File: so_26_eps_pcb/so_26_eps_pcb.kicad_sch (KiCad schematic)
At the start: 0 parts

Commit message: schematic: updated title block
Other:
- company: (none) -> Katharina Nilssen
- title: (none) -> so_26_eps_pcb
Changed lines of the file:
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@@
 	(generator_version "9.0")
 	(paper "A4")
+	(title_block
+		(title "so_26_eps_pcb")
+		(date "2026-01-28")
+		(rev "1")
+		(company "Katharina Nilssen")
+	)
 	(sheet_instances
 		(path "/"

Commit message: Laget symbol for LM22679TJ-ADJ/NOPB
Laget symbol for LM22679TJ-ADJ/NOPB
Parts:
- added C1, C2, C3, C4: C_Small, symbol Device:C_Small
- added L1: L_Small, symbol Device:L_Small
- added U1: LM22679TJ-ADJ/NOPB, symbol MySymbols:LM22679TJ-ADJ/NOPB

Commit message: Laget ferdig regulatorer
Mangler noen verdier
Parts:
- added R1, R2: R_Small, symbol Device:R_Small
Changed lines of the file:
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@@
+	)
+	(symbol
+		(lib_id "Device:R_Small")
+		(at 187.96 82.55 0)
+		(unit 1)
+		(exclude_from_sim no)
+		(in_bom yes)
+		(on_board yes)
+		(dnp no)
+		(fields_autoplaced yes)
+		(property "Reference" "R2"
+			(at 190.5 81.2799 0)
+			(effects
+				(font
+					(size 1.016 1.016)
+				)
+				(justify left)
+			)
+		)
+		(property "Value" "R_Small"
+			(at 190.5 83.8199 0)
+			(effects
+				(font
+					(size 1.27 1.27)
+				)
+				(justify left)
+			)
+		)
+		(property "Footprint" ""
+			(at 187.96 82.55 0)
+			(effects
+				(font
+					(size 1.27 1.27)
+				)
+				(hide yes)
+			)
+		)
+		(property "Datasheet" "~"
+			(at 187.96 82.55 0)
+			(effects
+				(font
+					(size 1.27 1.27)
+				)
+				(hide yes)
+			)
+		)
+		(property "Description" "Resistor, small symbol"
+			(at 187.96 82.55 0)
+			(effects
+				(font
+					(size 1.27 1.27)
+				)
+				(hide yes)
+			)
+		)
+		(pin "1"
+		)
+		(pin "2"
+		)
+		(instances
+			(project "so_26_eps_pcb"
+				(path "/bf42000f-dc59-47af-ab4a-8f583481d44f"
+					(reference "R2")
+					(unit 1)
+				)
+			)
+		)
 	)
 	(symbol
@@
 					(unit 1)
 				)
+			)
+		)
+	)
+	(symbol
+		(lib_id "Device:R_Small")
+		(at 187.96 67.31 0)
+		(unit 1)
+		(exclude_from_sim no)
+		(in_bom yes)
+		(on_board yes)
+		(dnp no)
+		(fields_autoplaced yes)
+		(property "Reference" "R1"
+			(at 190.5 66.0399 0)
+			(effects
+				(font
+					(size 1.016 1.016)
+				)
+				(justify left)
+			)
+		)
+		(property "Value" "R_Small"
+			(at 190.5 68.5799 0)
+			(effects
+				(font
+					(size 1.27 1.27)
+				)
+				(justify left)
+			)
+		)
+		(property "Footprint" ""
+			(at 187.96 67.31 0)
+			(effects
+				(font
+					(size 1.27 1.27)
+				)
+				(hide yes)
+			)
+		)
+		(property "Datasheet" "~"
+			(at 187.96 67.31 0)
+			(effects
+				(font
+					(size 1.27 1.27)
+				)
+				(hide yes)
+			)
+		)
+		(property "Description" "Resistor, small symbol"
+			(at 187.96 67.31 0)
+			(effects
+				(font
+					(size 1.27 1.27)
+				)
+				(hide yes)
+			)
+		)
+		(pin "1"
+		)
+		(pin "2"
+		)
+		(instances
+			(project ""
+				(path "/bf42000f-dc59-47af-ab4a-8f583481d44f"
+					(reference "R1")
+					(unit 1)
+				)

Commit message: Battery
Yuhhh
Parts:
- removed C2: C_Small, symbol Device:C_Small
- added 10VRegulator: LM22679TJ-ADJ/NOPB, symbol MySymbols:LM22679TJ-ADJ/NOPB
- added C2, C5: 100uF?, symbol Device:C_Polarized_Small
- added C6, C8: V, symbol Device:C_Polarized_Small
- added C7: 10 nF, symbol Device:C_Small
- added D1, D2: D_Schottky_Small, symbol Device:D_Schottky_Small
- added L2: 5,4 uH, symbol Device:L_Small
- added R3: 1,6kohm, symbol Device:R_Small
- added R4: R_Small, symbol Device:R_Small
- added R5: 909 ohm, symbol Device:R_Small
- added R6: 1kohm, symbol Device:R_Small
- C1, C3: value C_Small -> 1 uF
- C4: value C_Small -> 10 nF
- L1: value L_Small -> 3,5uH
- R1: value R_Small -> 1kohm
- renumbered U1 to 3V3Regulator
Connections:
- net GND: now also 3V3Regulator.4 (GND), C1.1, C3.1, R1.2, R2.2, 10VRegulator.4 (GND), C2.2, C5.2, C6.2, C8.2, D1.1 (K), D2.1 (K), R4.2, R6.2
- net at C1.2: now also 3V3Regulator.2 (SS)
- net at L1.1: now also 3V3Regulator.5 (SW), C4.2, D1.2 (A)
- net +3V3: now reaches L1.2
- net +3V3: now also C6.1, R3.2
- net at R2.1: now also 3V3Regulator.3 (IADJ)
- net at C4.1: now also 3V3Regulator.6 (BOOT)
- net at R1.1: now also 3V3Regulator.7 (FB), R3.1
- net at C3.2: now also 10VRegulator.2 (SS)
- net VBAT: now reaches 3V3Regulator.1 (VIN)
- net VBAT: now also 10VRegulator.1 (VIN), C2.1, C5.1
- new net: 10VRegulator.7 (FB), R5.1, R6.1
- new net: 10VRegulator.5 (SW), C7.2, D2.2 (A), L2.1
- new net: 10VRegulator.3 (IADJ), R4.1
- new net: 10VRegulator.6 (BOOT), C7.1
- new net +10V: C8.1, L2.2, R5.2
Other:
- moved on the sheet: C1, C4, L1, R1, R2

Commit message: Finished
The circuit design are finished!!!
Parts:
- added D3, D5, D6: LED_Small, symbol Device:LED_Small
- added D4: D_Schottky_Small, symbol Device:D_Schottky_Small
- added F1: Fuse_Small, symbol Device:Fuse_Small
- added J1: Conn_02x20_Counter_Clockwise, symbol Connector_Generic:Conn_02x20_Counter_Clockwise
- added JP1: SolderJumper_3_Open, symbol Jumper:SolderJumper_3_Open
- added R10, R11, R9: 909 ohm, symbol Device:R_Small
- added R12, R13: R_Small, symbol Device:R_Small
- added R7, R8: 0, symbol Device:R_Small
- added SW1: SW_SPDT, symbol Switch:SW_SPDT
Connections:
- net +10V: now also D3.2 (A), J1.38 (Pin_38), J1.39 (Pin_39), J1.40 (Pin_40), R7.1; no longer C8.1, L2.2, R5.2
- net +3V3: now also D4.1 (K), D6.2 (A), J1.33 (Pin_33), J1.34 (Pin_34); no longer C6.1, L1.2, R3.2
- net GND: now also D1.2 (A), D2.2 (A), J1.1 (Pin_1), J1.10 (Pin_10), J1.11 (Pin_11), J1.12 (Pin_12), J1.13 (Pin_13), J1.14 (Pin_14), J1.15 (Pin_15), J1.16 (Pin_16), J1.17 (Pin_17), J1.18 (Pin_18), J1.19 (Pin_19), J1.2 (Pin_2), J1.20 (Pin_20), J1.3 (Pin_3), J1.4 (Pin_4), J1.5 (Pin_5), J1.6 (Pin_6), J1.7 (Pin_7), J1.8 (Pin_8), J1.9 (Pin_9), R10.2, R11.2, R13.2, R9.2; no longer D1.1 (K), D2.1 (K)
- net VBAT: now also R12.1, SW1.2 (B)
- net at 10VRegulator.5 (SW), C7.2, L2.1: now also D2.1 (K); no longer D2.2 (A)
- net at 3V3Regulator.5 (SW), C4.2, L1.1: now also D1.1 (K); no longer D1.2 (A)
- new net: JP1.2 (C), R12.2, R13.1
- new net: D3.1 (K), R9.1
- new net: F1.2, SW1.1 (A)
- new net: D5.1 (K), R10.1
- new net: D6.1 (K), R11.1
- new net +10V_ALT: D5.2 (A), J1.35 (Pin_35), J1.36 (Pin_36), J1.37 (Pin_37), R8.1
- new net RADIO_RX: J1.32 (Pin_32)
- new net RADIO_TX: J1.31 (Pin_31)
- new net REG_+10V: C8.1, L2.2, R5.2, R7.2, R8.2
- new net REG_+3V3: C6.1, D4.2 (A), L1.2, R3.2
- new net VBAT_SENSE_0: J1.30 (Pin_30), JP1.1 (A)
- new net VBAT_SENSE_1: J1.29 (Pin_29), JP1.3 (B)
- no-connect marks 0 -> 9
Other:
- moved on the sheet: D1, D2

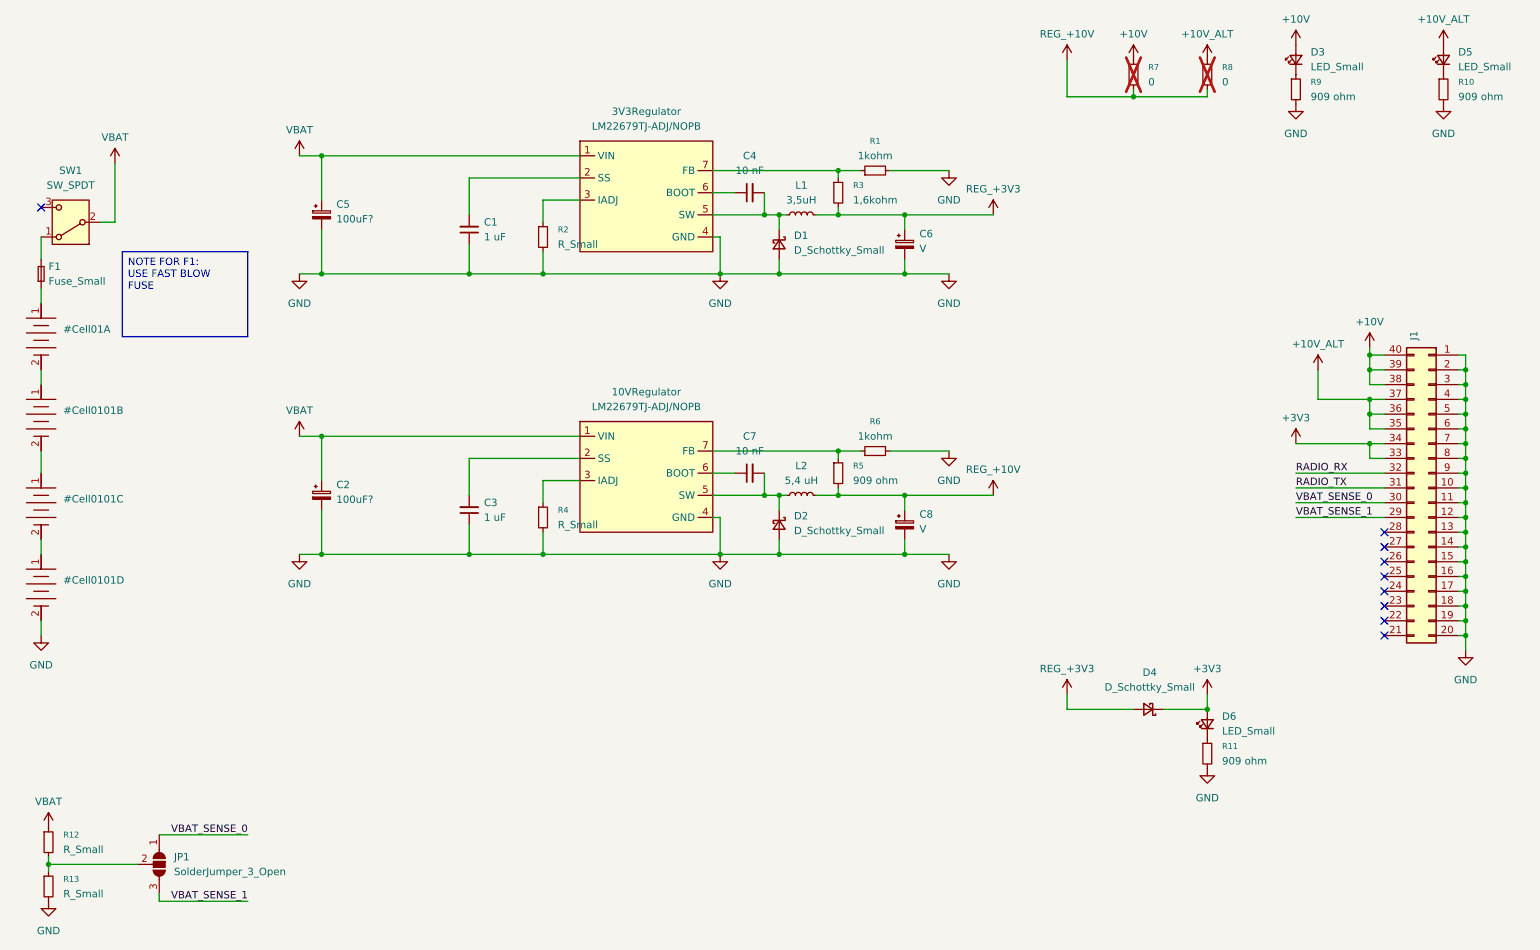
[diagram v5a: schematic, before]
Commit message: checked by aj
schematic
- fixed symbols and added capacitors

pcb
- added outline and stack + some footprints
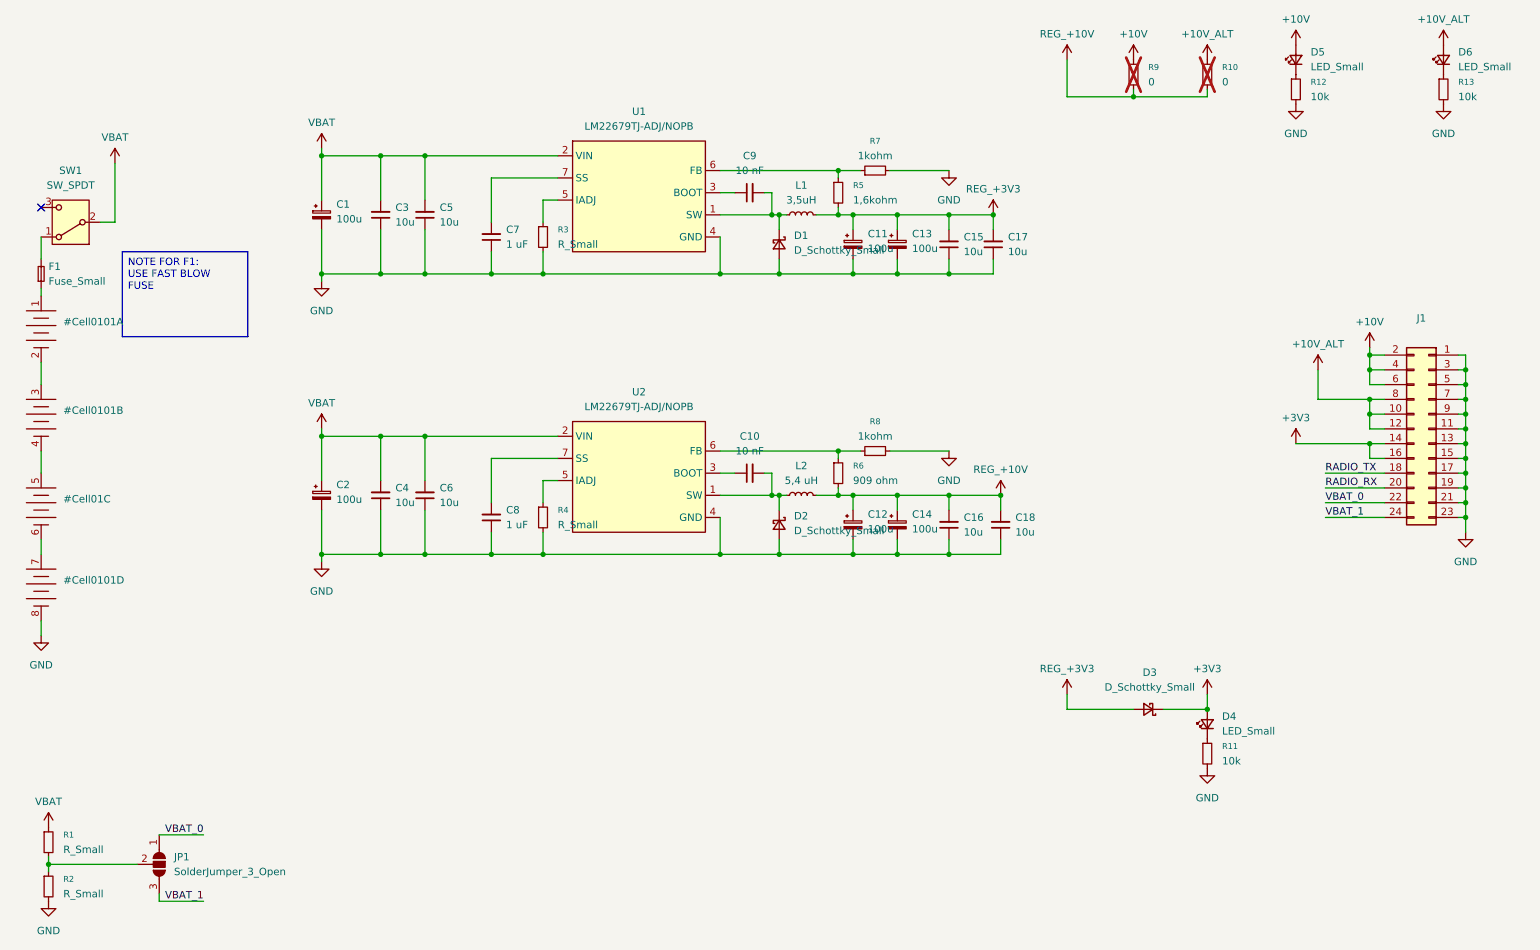
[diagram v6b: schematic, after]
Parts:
- removed 10VRegulator, 3V3Regulator: LM22679TJ-ADJ/NOPB, symbol MySymbols:LM22679TJ-ADJ/NOPB
- removed C1: 1 uF, symbol Device:C_Small
- removed C8: V, symbol Device:C_Polarized_Small
- removed J1: Conn_02x20_Counter_Clockwise, symbol Connector_Generic:Conn_02x20_Counter_Clockwise
- added C12, C13, C14: 100u, Capacitor_THT:CP_Radial_D6.3mm_P2.50mm, symbol Device:C_Polarized_Small
- added C15, C16, C17, C18, C3, C4, C5, C6: 10u, Capacitor_SMD:C_1206_3216Metric_Pad1.33x1.80mm_HandSolder, symbol Device:C_Small
- added C7: 1 uF, Capacitor_SMD:C_1206_3216Metric_Pad1.33x1.80mm_HandSolder, symbol Device:C_Small
- added J1: Conn_02x12_Odd_Even, Connector_PinSocket_2.54mm:PinSocket_2x12_P2.54mm_Vertical, symbol Connector_Generic:Conn_02x12_Odd_Even
- added U1, U2: LM22679TJ-ADJ/NOPB, Package_TO_SOT_SMD:TO-263-7_TabPin4, symbol MySymbols:LM22679TJ-ADJ/NOPB
- C1: renamed from C5; value 100uF? -> 100u; footprint (none) -> Capacitor_THT:CP_Radial_D6.3mm_P2.50mm
- C10: renamed from C7; footprint (none) -> Capacitor_SMD:C_0805_2012Metric_Pad1.18x1.45mm_HandSolder
- C11: renamed from C6; value V -> 100u; footprint (none) -> Capacitor_THT:CP_Radial_D6.3mm_P2.50mm
- C2: value 100uF? -> 100u; footprint (none) -> Capacitor_THT:CP_Radial_D6.3mm_P2.50mm
- C8: renamed from C3; footprint (none) -> Capacitor_SMD:C_1206_3216Metric_Pad1.33x1.80mm_HandSolder
- C9: renamed from C4; footprint (none) -> Capacitor_SMD:C_0805_2012Metric_Pad1.18x1.45mm_HandSolder
- D4: renamed from D6; footprint (none) -> LED_SMD:LED_0805_2012Metric_Pad1.15x1.40mm_HandSolder
- D5: renamed from D3; footprint (none) -> LED_SMD:LED_0805_2012Metric_Pad1.15x1.40mm_HandSolder
- D6: renamed from D5; footprint (none) -> LED_SMD:LED_0805_2012Metric_Pad1.15x1.40mm_HandSolder
- JP1: footprint (none) -> Jumper:SolderJumper-3_P2.0mm_Open_TrianglePad1.0x1.5mm_NumberLabels
- R1: renamed from R12; footprint (none) -> Resistor_SMD:R_0805_2012Metric_Pad1.20x1.40mm_HandSolder
- R10: renamed from R8; footprint (none) -> Resistor_SMD:R_0805_2012Metric_Pad1.20x1.40mm_HandSolder
- R11: value 909 ohm -> 10k; footprint (none) -> Resistor_SMD:R_0805_2012Metric_Pad1.20x1.40mm_HandSolder
- R12: renamed from R9; value 909 ohm -> 10k; footprint (none) -> Resistor_SMD:R_0805_2012Metric_Pad1.20x1.40mm_HandSolder
- R13: renamed from R10; value 909 ohm -> 10k; footprint (none) -> Resistor_SMD:R_0805_2012Metric_Pad1.20x1.40mm_HandSolder
- R2: renamed from R13; footprint (none) -> Resistor_SMD:R_0805_2012Metric_Pad1.20x1.40mm_HandSolder
- R3: renamed from R2; footprint (none) -> Resistor_SMD:R_0805_2012Metric_Pad1.20x1.40mm_HandSolder
- R4: footprint (none) -> Resistor_SMD:R_0805_2012Metric_Pad1.20x1.40mm_HandSolder
- R5: renamed from R3; footprint (none) -> Resistor_SMD:R_0805_2012Metric_Pad1.20x1.40mm_HandSolder
- R6: renamed from R5; footprint (none) -> Resistor_SMD:R_0805_2012Metric_Pad1.20x1.40mm_HandSolder
- R7: renamed from R1; footprint (none) -> Resistor_SMD:R_0805_2012Metric_Pad1.20x1.40mm_HandSolder
- R8: renamed from R6; footprint (none) -> Resistor_SMD:R_0805_2012Metric_Pad1.20x1.40mm_HandSolder
- R9: renamed from R7; footprint (none) -> Resistor_SMD:R_0805_2012Metric_Pad1.20x1.40mm_HandSolder
- renumbered D4 to D3
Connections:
- net +10V: now also J1.2 (Pin_2), J1.4 (Pin_4), J1.6 (Pin_6)
- net +10V_ALT: now also J1.10 (Pin_10), J1.12 (Pin_12), J1.8 (Pin_8)
- net +3V3: now also J1.14 (Pin_14), J1.16 (Pin_16)
- net GND: now also C12.2, C13.2, C14.2, C15.1, C16.1, C17.1, C18.1, C3.1, C4.1, C5.1, C6.1, C7.1, J1.1 (Pin_1), J1.11 (Pin_11), J1.13 (Pin_13), J1.15 (Pin_15), J1.17 (Pin_17), J1.19 (Pin_19), J1.21 (Pin_21), J1.23 (Pin_23), J1.3 (Pin_3), J1.5 (Pin_5), J1.7 (Pin_7), J1.9 (Pin_9), U1.4 (GND), U2.4 (GND)
- net RADIO_RX: now also J1.20 (Pin_20)
- net RADIO_TX: now also J1.18 (Pin_18)
- net REG_+10V: now also C12.1, C14.1, C16.2, C18.2
- net REG_+3V3: now also C13.1, C15.2, C17.2
- net VBAT: now also C3.2, C4.2, C5.2, C6.2, U1.2 (VIN), U2.2 (VIN)
- net at R6.1, R8.1: now also U2.6 (FB)
- net at C10.2, D2.1 (K), L2.1: now also U2.1 (SW)
- net at R4.1: now also U2.5 (IADJ)
- net at C9.2, D1.1 (K), L1.1: now also U1.1 (SW)
- net at C10.1: now also U2.3 (BOOT)
- net at R3.1: now also U1.5 (IADJ)
- net at R5.1, R7.1: now also U1.6 (FB)
- net at C9.1: now also U1.3 (BOOT)
- net at C8.2: now also U2.7 (SS)
- net VBAT_SENSE_0 renamed VBAT_0
- net VBAT_0: now also J1.22 (Pin_22)
- net VBAT_SENSE_1 renamed VBAT_1
- net VBAT_1: now also J1.24 (Pin_24)
- new net: C7.2, U1.7 (SS)
- no-connect marks 9 -> 1
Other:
- moved on the sheet: C11, C8

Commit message: Added test points
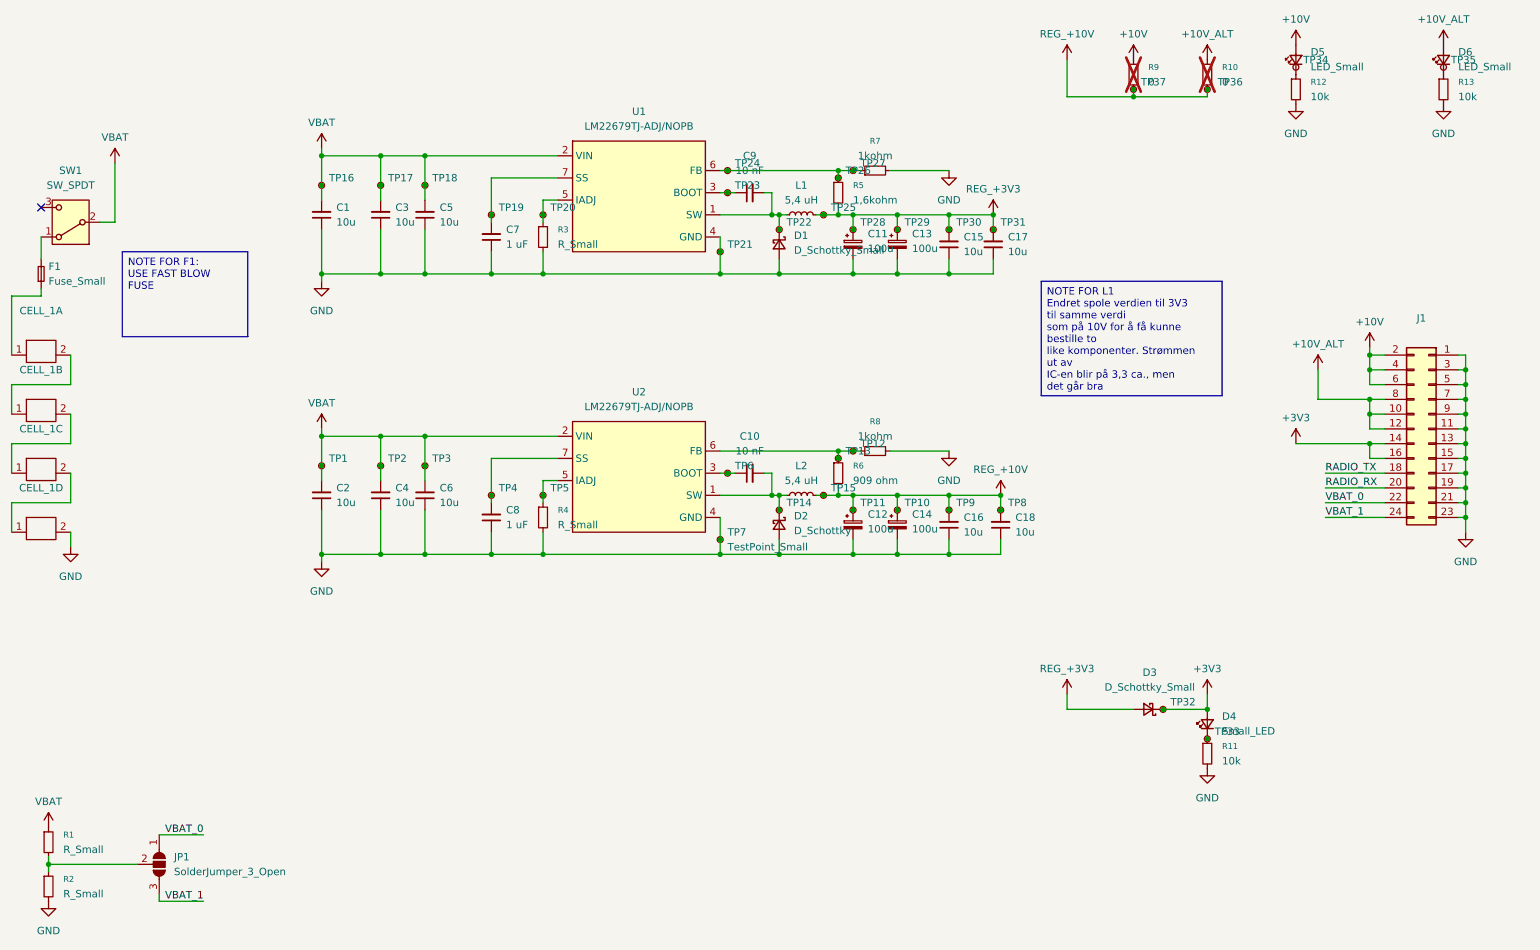
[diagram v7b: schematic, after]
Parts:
- removed C1, C2: 100u, Capacitor_THT:CP_Radial_D6.3mm_P2.50mm, symbol Device:C_Polarized_Small
- added C1, C2: 10u, Capacitor_SMD:C_1206_3216Metric_Pad1.33x1.80mm_HandSolder, symbol Device:C_Small
- added CELL_1: ~, symbol MySymbols:Battery_18650_boxes
- added TP1, TP10, TP11, TP12, TP13, TP14, TP15, TP16, TP17, TP18, TP19, TP2, TP20, TP21, TP22, TP23, TP24, TP25, TP26, TP27, TP28, TP29, TP3, TP30, TP31, TP32, TP33, TP34, TP35, TP36, TP37, TP4, TP5, TP6, TP8, TP9: ~, symbol Connector:TestPoint_Small
- added TP7: TestPoint_Small, symbol Connector:TestPoint_Small
- D2: value D_Schottky_Small -> D_Schottky
- D4: value LED_Small -> Small_LED
- L1: value 3,5uH -> 5,4 uH
- R10, R9: footprint Resistor_SMD:R_0805_2012Metric_Pad1.20x1.40mm_HandSolder -> Resistor_SMD:R_2512_6332Metric_Pad1.40x3.35mm_HandSolder
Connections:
- net +3V3: now also TP32.1
- net GND: now also C1.1, C2.1, CELL_1.2, TP21.1, TP7.1
- net REG_+10V: now also TP10.1, TP11.1, TP15.1, TP36.1, TP37.1, TP8.1, TP9.1
- net REG_+3V3: now also TP25.1, TP28.1, TP29.1, TP30.1, TP31.1
- net VBAT: now also C1.2, C2.2, TP1.1, TP16.1, TP17.1, TP18.1, TP2.1, TP3.1
- net at R6.1, R8.1, U2.6 (FB): now also TP12.1, TP13.1
- net at C10.2, D2.1 (K), L2.1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: now also TP14.1
- net at R4.1, U2.5 (IADJ): now also TP5.1
- net at C9.2, D1.1 (K), L1.1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: now also TP22.1
- net at C9.1, U1.3 (BOOT): now also TP23.1
- net at R3.1, U1.5 (IADJ): now also TP20.1
- net at R5.1, R7.1, U1.6 (FB): now also TP24.1, TP26.1, TP27.1
- net at C7.2, U1.7 (SS): now also TP19.1
- net at C10.1, U2.3 (BOOT): now also TP6.1
- net at C8.2, U2.7 (SS): now also TP4.1
- net at F1.1: now also CELL_1.1
- net at D4.1 (K), R11.1: now also TP33.1
- new net: CELL_1.1, CELL_1.2 (x3)
